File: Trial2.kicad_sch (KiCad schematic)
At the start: 3 parts, among them J1 Barrel_Jack_Switch

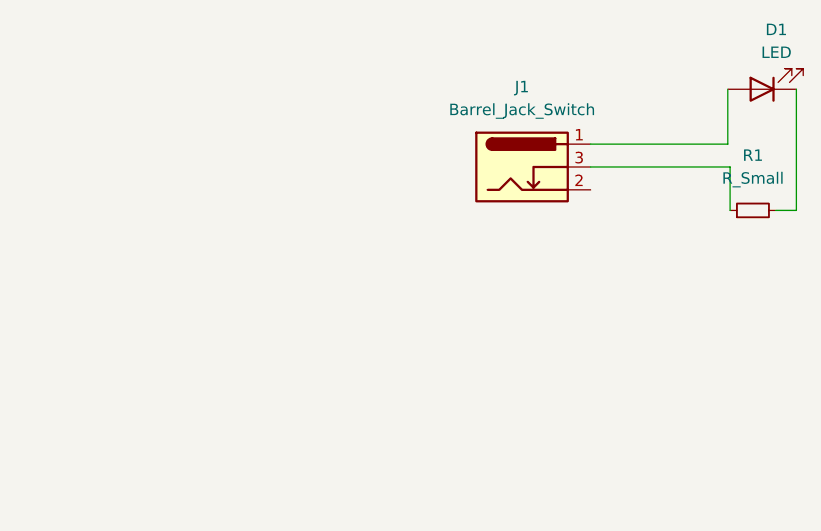
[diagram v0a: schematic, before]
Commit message: Circuit Edits
I added a Molex connector 01x03 and a Switch
I added footprints for the connector and the Switch
I added the sheet info
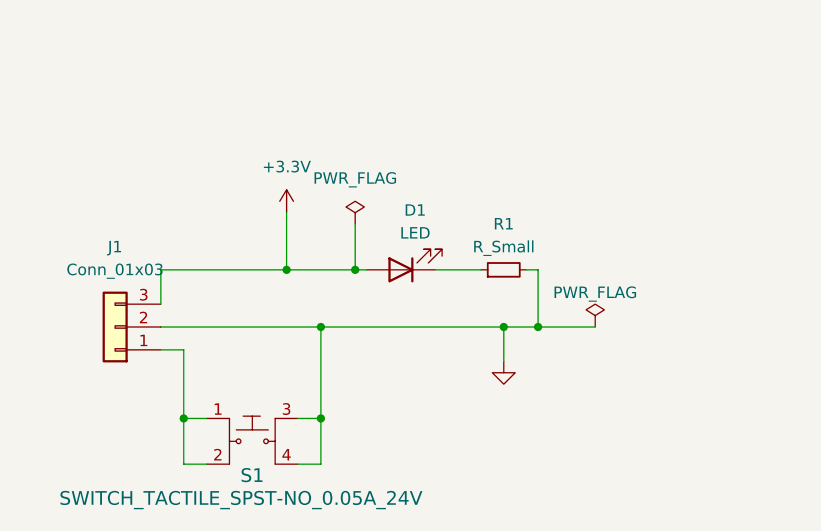
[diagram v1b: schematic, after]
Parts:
- removed J1: Barrel_Jack_Switch, Button_Switch_THT:KSA_Tactile_SPST, symbol Connector:Barrel_Jack_Switch
- added J1: Conn_01x03, Connector_Molex:Molex_KK-254_AE-6410-03A_1x03_P2.54mm_Vertical, symbol Connector_Generic:Conn_01x03
- added S1: SWITCH_TACTILE_SPST-NO_0.05A_24V, Button_Switch_SMD:SW_SPST_TL3342, symbol GPAD_SCH_LIB:SWITCH_TACTILE_SPST-NO_0.05A_24V
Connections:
- net +3.3V: now reaches D1.2 (A)
- net +3.3V: now also J1.3 (Pin_3)
- net at R1.1: now also D1.1 (K)
- net GND: now reaches R1.2
- net GND: now also J1.2 (Pin_2), S1.3, S1.4; no longer D1.1 (K)
- new net: J1.1 (Pin_1), S1.1, S1.2
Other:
- company: (none) -> PubInv Volunteers
- title: (none) -> ON OFF LAMP CIRCUIT
- moved on the sheet: D1, R1

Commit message: Added gbr and pos files.
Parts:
- D1: JLCPCB Part # (none) -> C19189746
- J1: JLCPCB Part # C505296 -> C24980
- R1: JLCPCB Part # (none) -> C2129186
- S1: JLCPCB Part # (none) -> C318884
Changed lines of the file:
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@@
       (effects (font (size 1.27 1.27)) hide)
     )
-    (property "JLCPCB Part #" "C505296" (at 35.56 92.71 0)
+    (property "JLCPCB Part #" "C24980" (at 35.56 92.71 0)
       (effects (font (size 1.27 1.27)) hide)
     )
@@
       (effects (font (size 1.27 1.27)) hide)
     )
+    (property "JLCPCB Part #" "C318884" (at 50.8 105.41 0)
+      (effects (font (size 1.27 1.27)) hide)
+    )
     (pin "1")
     (pin "2")
@@
       (effects (font (size 1.27 1.27)) hide)
     )
+    (property "JLCPCB Part #" "C19189746" (at 67.31 86.36 0)
+      (effects (font (size 1.27 1.27)) hide)
+    )
     (pin "1")
     (pin "2")
@@
       (effects (font (size 1.27 1.27)) hide)
     )
+    (property "JLCPCB Part #" "C2129186" (at 78.74 86.36 0)
+      (effects (font (size 1.27 1.27)) hide)
+    )
